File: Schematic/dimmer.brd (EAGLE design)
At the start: 66 x 40.6 mm, 18 parts, among them Q1 IRF840, T1 BC547

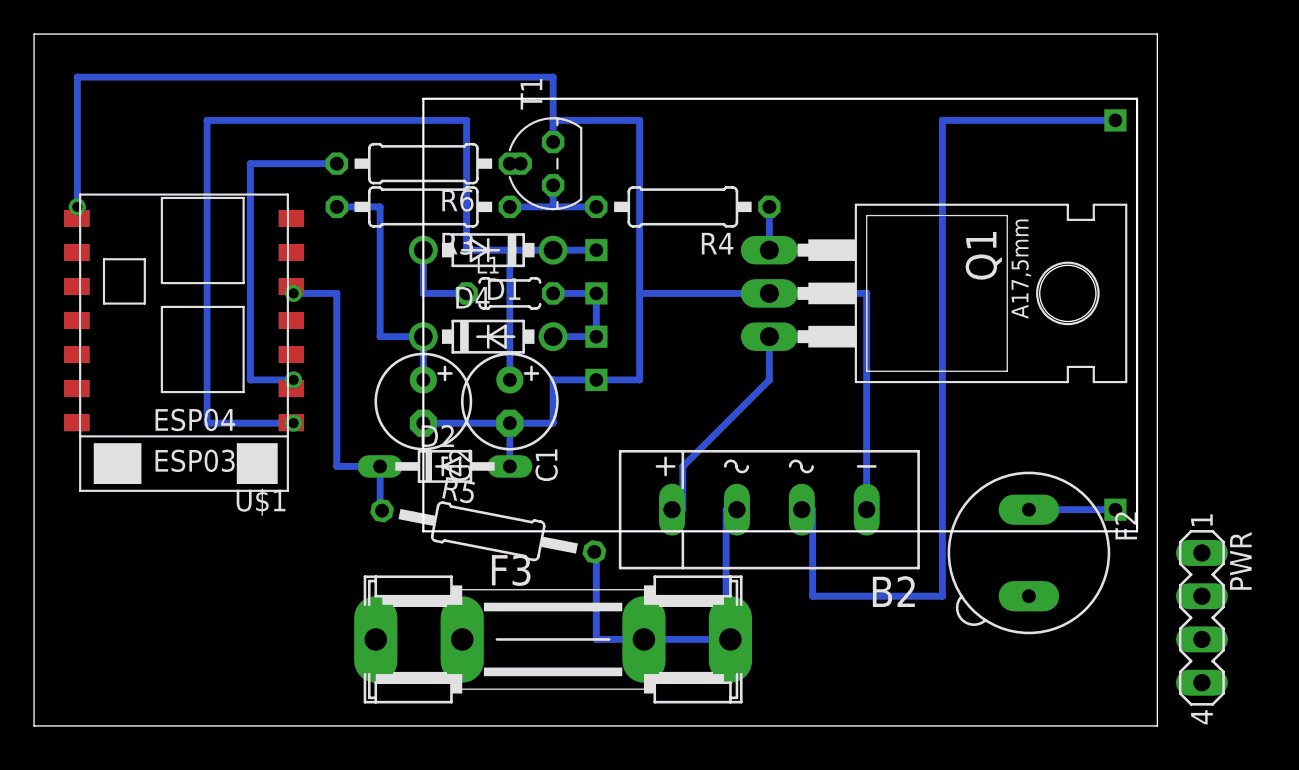
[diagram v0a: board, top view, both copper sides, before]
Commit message: Add SMPS with correct dimmensions
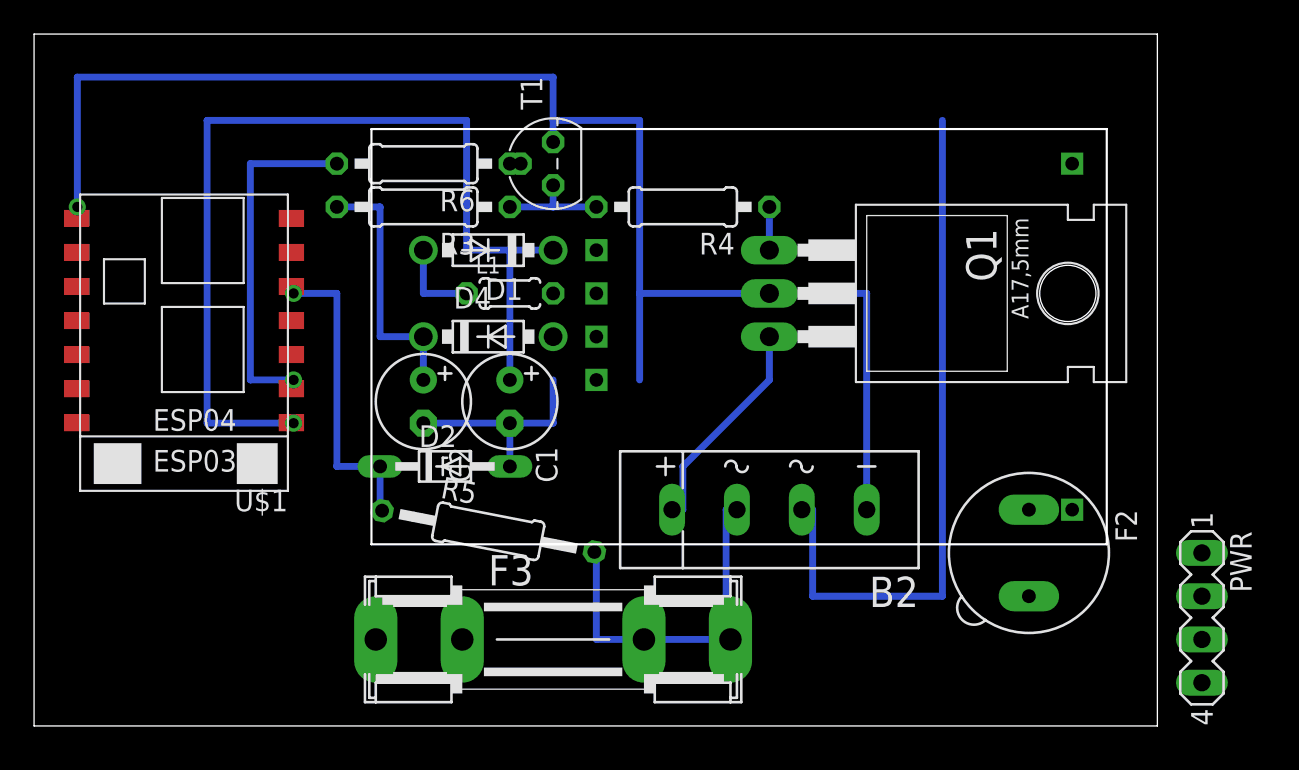
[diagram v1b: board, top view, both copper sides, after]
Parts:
- moved U$2 28.4 mm to (40.6, 22.9)
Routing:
- net N$4: track 51.4 -> 41.3 mm
- net N$6: track 7.62 -> 0.00 mm
- net GND: track 104.2 -> 99.1 mm
- net N$9: track 5.08 -> 0.00 mm
- net +3V3: track 61.1 -> 58.6 mm
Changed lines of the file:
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@@
 <element name="U$1" library="esp8266modules" package="ESP-03" value="ESP8266" x="9.906" y="22.606" rot="R180"/>
 <element name="T1" library="transistor" package="TO92" value="BC547" x="30.48" y="33.02" rot="R90"/>
-<element name="U$2" library="smps" package="SMPS" value="SMPS" x="66.04" y="10.16" rot="R180"/>
 <element name="D1" library="diode" package="DO41-7.6" value="1N5817-B" x="26.67" y="27.94" rot="R180"/>
 <element name="D4" library="diode" package="DO41-7.6" value="1N5817-B" x="26.67" y="22.86"/>
@@
 <attribute name="OC_FARNELL" value="unknown" x="30.48" y="5.08" size="1.778" layer="27" display="off"/>
 </element>
+<element name="U$2" library="smps" package="SMPS" value="SMPS" x="40.64" y="22.86" rot="R180"/>
 </elements>
 <signals>
@@
 <contactref element="C1" pad="+"/>
 <contactref element="U$1" pad="VCC"/>
-<contactref element="U$2" pad="FB"/>
 <contactref element="D1" pad="C"/>
-<wire x1="33.02" y1="27.94" x2="30.48" y2="27.94" width="0.4064" layer="16"/>
 <wire x1="27.94" y1="20.32" x2="27.94" y2="27.94" width="0.4064" layer="16"/>
 <wire x1="27.94" y1="27.94" x2="30.48" y2="27.94" width="0.4064" layer="16"/>
@@
 <wire x1="25.4" y1="35.56" x2="25.4" y2="27.94" width="0.4064" layer="16"/>
 <wire x1="25.4" y1="27.94" x2="27.94" y2="27.94" width="0.4064" layer="16"/>
+<contactref element="U$2" pad="FB"/>
+<wire x1="33.02" y1="27.94" x2="27.94" y2="20.32" width="0" layer="19" extent="1-1"/>
 </signal>
 <signal name="GND">
@@
 <contactref element="Q1" pad="2"/>
 <contactref element="T1" pad="1"/>
-<contactref element="U$2" pad="GND"/>
 <wire x1="22.86" y1="17.78" x2="27.94" y2="17.78" width="0.4064" layer="16"/>
 <wire x1="27.94" y1="17.78" x2="30.48" y2="17.78" width="0.4064" layer="16"/>
 <wire x1="30.48" y1="17.78" x2="30.48" y2="20.32" width="0.4064" layer="16"/>
-<wire x1="30.48" y1="20.32" x2="33.02" y2="20.32" width="0.4064" layer="16"/>
-<wire x1="33.02" y1="20.32" x2="35.56" y2="20.32" width="0.4064" layer="16"/>
 <wire x1="35.56" y1="20.32" x2="35.56" y2="25.4" width="0.4064" layer="16"/>
 <wire x1="35.56" y1="25.4" x2="43.18" y2="25.4" width="0.4064" layer="16"/>
@@
 <wire x1="2.54" y1="30.48" x2="2.54" y2="38.1" width="0.4064" layer="16"/>
 <wire x1="2.54" y1="38.1" x2="30.48" y2="38.1" width="0.4064" layer="16"/>
+<contactref element="U$2" pad="GND"/>
+<wire x1="35.56" y1="20.32" x2="30.48" y2="20.32" width="0" layer="19" extent="16-16"/>
+<wire x1="33.02" y1="20.32" x2="27.94" y2="15.24" width="0" layer="19" extent="1-1"/>
 </signal>
 <signal name="N$17">
@@
 <contactref element="F2" pad="1"/>
 <contactref element="U$2" pad="L"/>
-<wire x1="63.5" y1="12.7" x2="58.42" y2="12.7" width="0.4064" layer="16"/>
+<wire x1="60.96" y1="12.7" x2="58.42" y2="12.7" width="0" layer="19" extent="1-1"/>
 </signal>
 <signal name="N$12">
@@
 <signal name="N$6">
 <contactref element="L1" pad="2"/>
+<contactref element="D4" pad="A"/>
 <contactref element="U$2" pad="VPP2"/>
 <contactref element="U$2" pad="VPP1"/>
-<contactref element="D4" pad="A"/>
-<wire x1="30.48" y1="25.4" x2="33.02" y2="25.4" width="0.4064" layer="16"/>
-<wire x1="30.48" y1="22.86" x2="33.02" y2="22.86" width="0.4064" layer="16"/>
-<wire x1="33.02" y1="22.86" x2="33.02" y2="25.4" width="0.4064" layer="16"/>
+<wire x1="30.48" y1="22.86" x2="30.48" y2="25.4" width="0" layer="19" extent="1-1"/>
+<wire x1="33.02" y1="22.86" x2="30.48" y2="22.86" width="0" layer="19" extent="1-1"/>
+<wire x1="33.02" y1="25.4" x2="33.02" y2="22.86" width="0" layer="19" extent="1-1"/>
 </signal>
 <signal name="+5V">
@@
 <signal name="N$4">
 <contactref element="PWR" pad="1"/>
-<contactref element="U$2" pad="N"/>
 <contactref element="B2" pad="AC1"/>
-<wire x1="63.5" y1="35.56" x2="53.34" y2="35.56" width="0.4064" layer="16"/>
 <wire x1="53.34" y1="35.56" x2="53.34" y2="7.62" width="0.4064" layer="16"/>
 <wire x1="53.34" y1="7.62" x2="45.72" y2="7.62" width="0.4064" layer="16"/>
 <wire x1="45.72" y1="7.62" x2="45.72" y2="12.7" width="0.4064" layer="16"/>
 <wire x1="45.72" y1="12.7" x2="45.085" y2="12.7" width="0.4064" layer="16"/>
+<contactref element="U$2" pad="N"/>
 <wire x1="53.34" y1="7.62" x2="68.58" y2="10.16" width="0" layer="19" extent="16-16"/>
+<wire x1="60.96" y1="33.02" x2="45.72" y2="7.62" width="0" layer="19" extent="16-16"/>
 </signal>
 <signal name="N$5">

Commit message: Add L dimension
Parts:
- D4: value 1N5817-B -> 1N4148
- L1: value (none) -> 330n
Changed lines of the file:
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@@
 <element name="C1" library="rcl" package="E2,5-6" value="10u/16" x="27.94" y="19.05" rot="R270"/>
 <element name="C2" library="rcl" package="E2,5-6" value="10u/16" x="22.86" y="19.05" rot="R270"/>
-<element name="L1" library="rcl" package="0204/5" value="" x="27.94" y="25.4"/>
+<element name="L1" library="rcl" package="0204/5" value="330n" x="27.94" y="25.4"/>
 <element name="U$1" library="esp8266modules" package="ESP-03" value="ESP8266" x="9.906" y="22.606" rot="R180"/>
 <element name="T1" library="transistor" package="TO92" value="BC547" x="30.48" y="33.02" rot="R90"/>
 <element name="D1" library="diode" package="DO41-7.6" value="1N5817-B" x="26.67" y="27.94" rot="R180"/>
-<element name="D4" library="diode" package="DO41-7.6" value="1N5817-B" x="26.67" y="22.86"/>
+<element name="D4" library="diode" package="DO41-7.6" value="1N4148" x="26.67" y="22.86"/>
 <element name="F3" library="fuse" package="SHK20L" value="1A flink" x="30.48" y="5.08">
 <attribute name="MF" value="" x="30.48" y="5.08" size="1.778" layer="27" display="off"/>
